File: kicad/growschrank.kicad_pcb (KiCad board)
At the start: 2 copper layers, 68.6 x 53.3 mm, 14 parts, among them J1 OLED, J2 BME280, J3 ESP8266, J4 DS3231, J5 Relais, J6 Rotary_Encoder, P1 Power, P2 Analog, P3 Digital, P4 Digital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

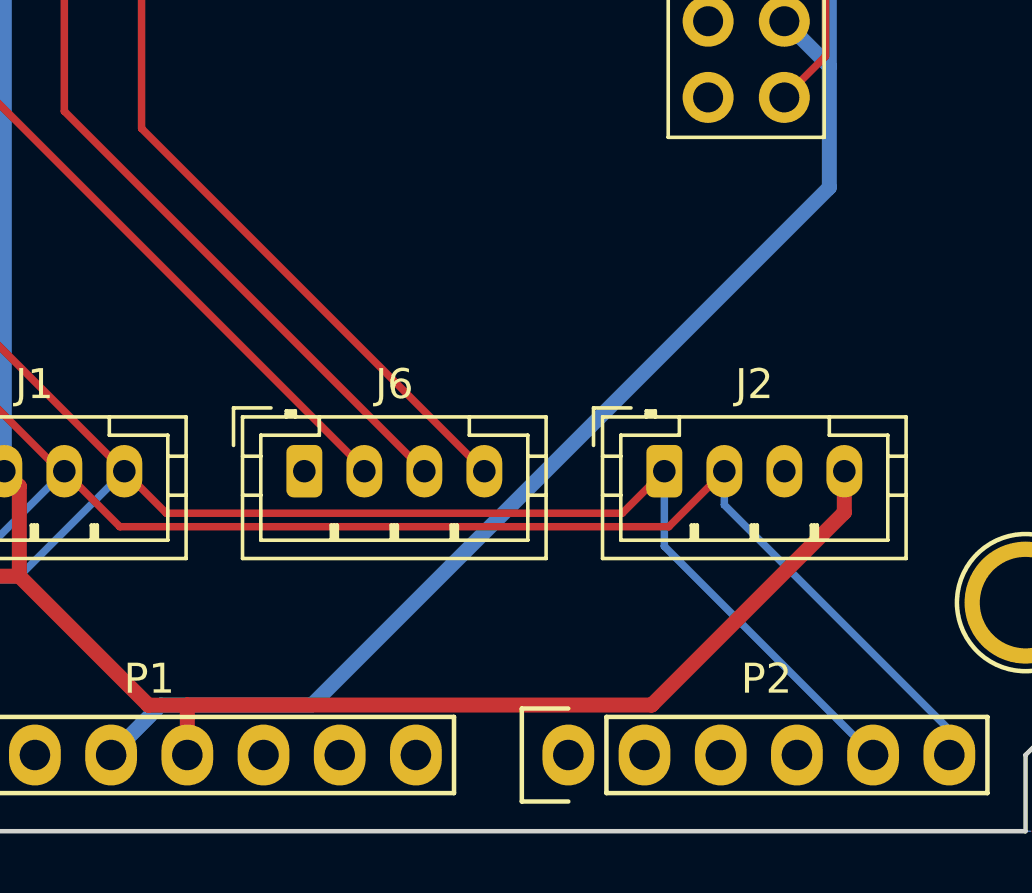
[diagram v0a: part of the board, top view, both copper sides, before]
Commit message: Fixed power supply of BME280
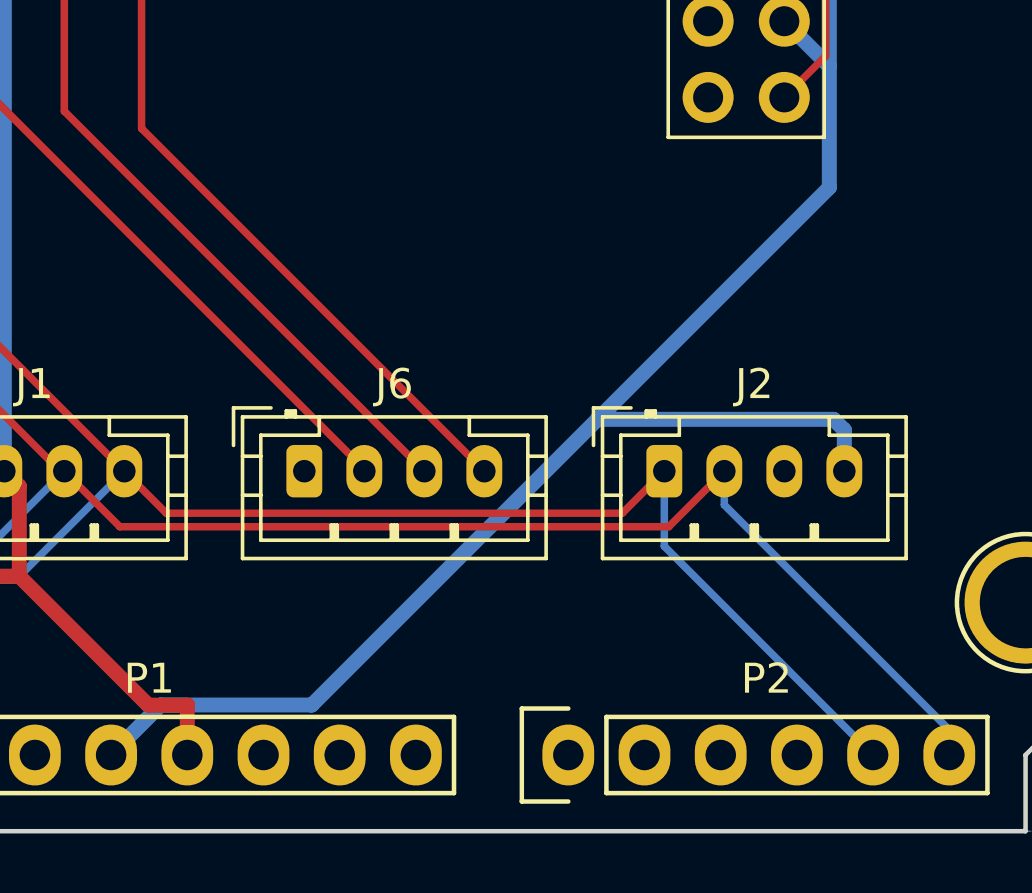
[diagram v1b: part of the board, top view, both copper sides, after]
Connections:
- J2 pad 4: +5V -> +3V3
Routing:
- net +5V: track 98.8 -> 72.9 mm
- net +3V3: track 45.1 -> 54.9 mm

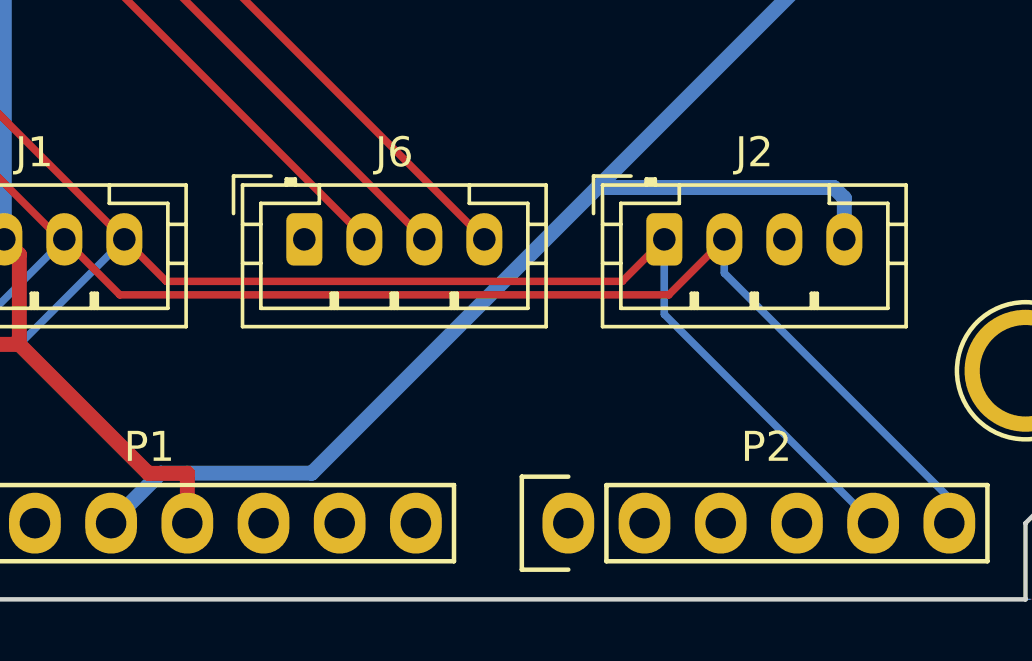
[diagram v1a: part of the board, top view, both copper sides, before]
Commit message: GY-BME280 is 3.3V-5V fuck this shit
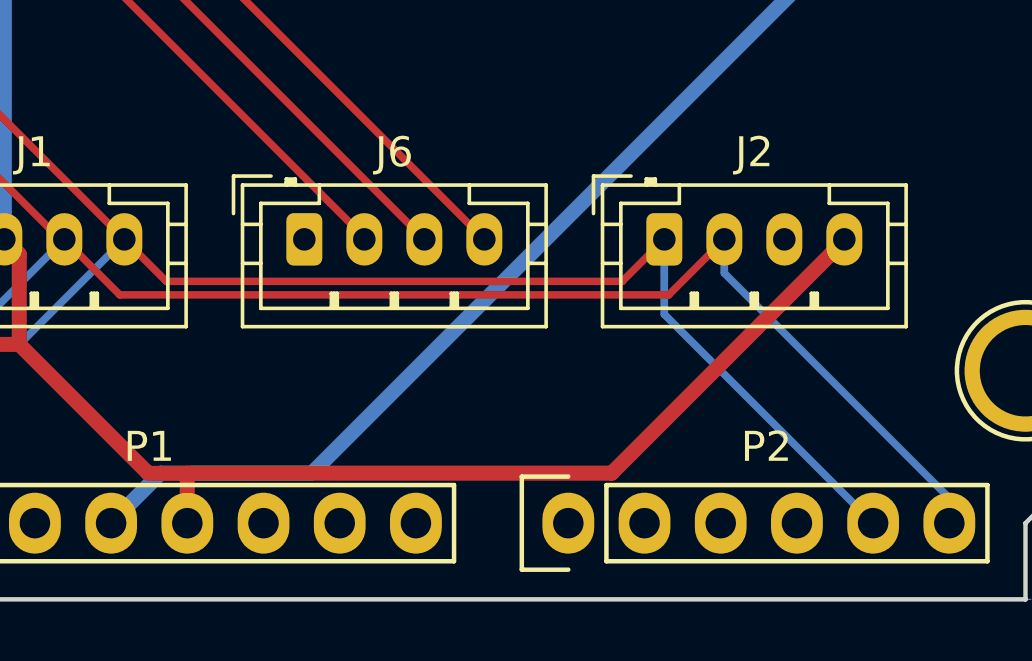
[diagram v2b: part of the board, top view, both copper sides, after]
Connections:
- J2 pad 4: +3V3 -> +5V
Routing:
- net +5V: track 72.9 -> 98.5 mm
- net +3V3: track 54.9 -> 45.1 mm

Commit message: Changed relais connector
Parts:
- J1, J2, J6: footprint Connector_JST:JST_PH_B4B-PH-K_1x04_P2.00mm_Vertical -> Connector_JST:JST_XH_B4B-XH-A_1x04_P2.50mm_Vertical
- J5: footprint Connector_PinHeader_2.54mm:PinHeader_1x10_P2.54mm_Vertical -> Connector_JST:JST_XH_B10B-XH-A_1x10_P2.50mm_Vertical
- moved J5 41.0 mm to (133.5, 83.4), turned to 0 degrees
- moved J2 31.1 mm to (162.0, 83.4)
- moved J1 3.50 mm to (137.5, 114.4)
- moved J6 2.00 mm to (151.0, 114.4)
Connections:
- J5 pad 1: GND -> +5V
- J5 pad 10: +5V -> GND
- J5 pad 2: /2 -> /9(**)
- J5 pad 3: /3(**) -> /8
- J5 pad 4: /4 -> /7
- J5 pad 5: /5(**) -> /6(**)
- J5 pad 6: /6(**) -> /5(**)
- J5 pad 7: /7 -> /4
- J5 pad 8: /8 -> /3(**)
- J5 pad 9: /9(**) -> /2
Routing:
- net /2: track 9.52 -> 20.2 mm
- net /4: track 9.66 -> 19.9 mm
- net /3(**): track 9.74 -> 19.9 mm
- net +5V: track 98.5 -> 108.6 mm
- net /7: track 10.1 -> 19.7 mm
- net /6(**): track 10.2 -> 19.7 mm
- net /5(**): track 10.9 -> 19.7 mm
- net /9(**): track 10.7 -> 18.7 mm
- net /8: track 10.7 -> 18.2 mm
- net +3V3: track 45.1 -> 50.8 mm
- net /A5(SCL): track 105.6 -> 103.1 mm
- net /A4(SDA): track 105.6 -> 103.2 mm, vias 0 -> 1
- net /0(Rx): track 30.0 -> 28.6 mm
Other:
- board text added: "growschrank rev1.1 by Elias Kleimeier"

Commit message: Added more space for clock
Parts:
- moved J2 3.50 mm to (165.5, 83.4)
- moved J5 3.50 mm to (137.0, 83.4)
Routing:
- net /9(**): track 18.7 -> 14.0 mm
- net /4: track 19.9 -> 15.5 mm
- net /3(**): track 19.9 -> 15.5 mm
- net /7: track 19.7 -> 15.5 mm
- net /8: track 18.2 -> 14.1 mm
- net /6(**): track 19.7 -> 16.2 mm
- net /5(**): track 19.7 -> 16.2 mm
- net /2: track 20.2 -> 16.7 mm
- net +5V: track 108.6 -> 106.7 mm
- net /1(Tx): track 22.1 -> 23.8 mm
- net /0(Rx): track 28.6 -> 30.0 mm
- net /A5(SCL): track 103.1 -> 104.4 mm
- net /12(MISO): track 43.7 -> 42.8 mm
- net /10(**/SS): track 43.5 -> 42.8 mm
